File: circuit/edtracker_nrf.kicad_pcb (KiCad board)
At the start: 2 copper layers, 50 x 44 mm, 20 parts, among them M1 NRF24LE1_SMALL, Q1 TPS1101D, SW1 SW_PUSH, SW2 SWITCH_INV, U1 NRF24LE1_PROG, U2 MPU-6050, U3 UART

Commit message: 
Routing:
- net (no net): track 0.00 -> 170.0 mm
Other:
- board text added: "B"
- board text added: "F"

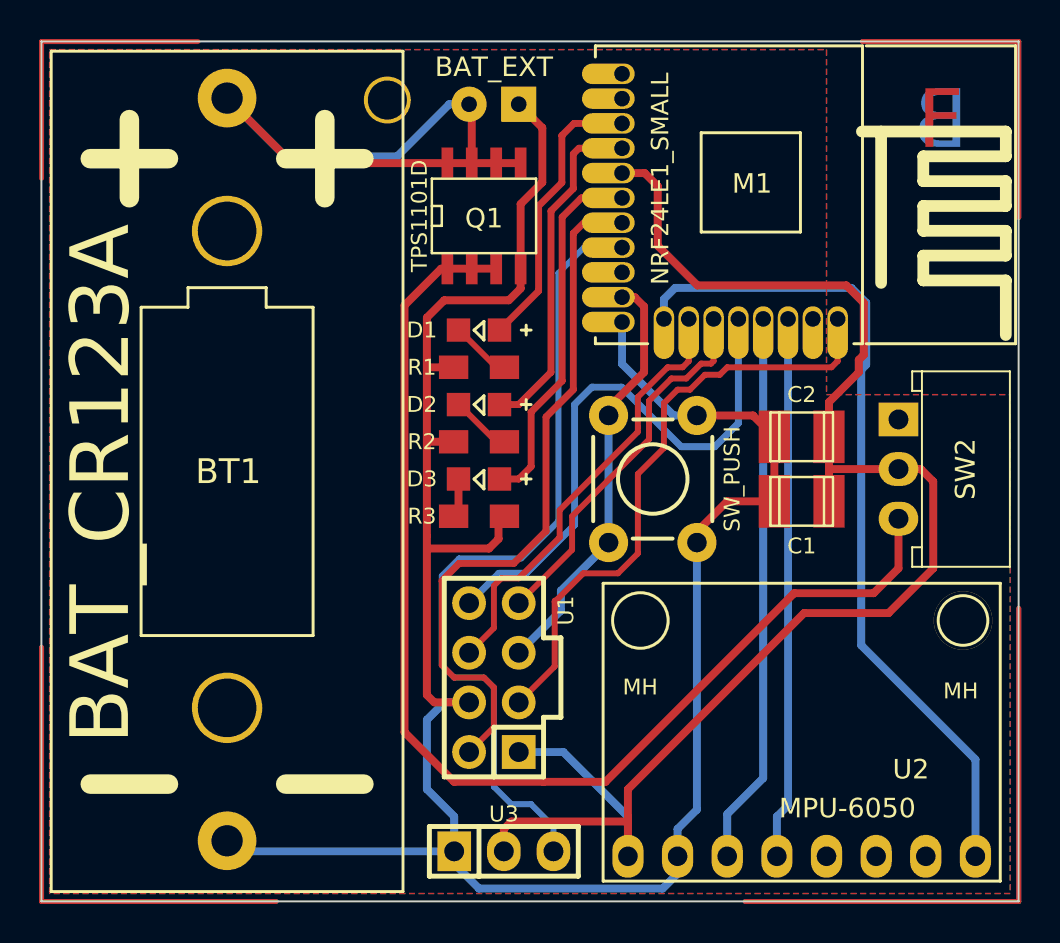
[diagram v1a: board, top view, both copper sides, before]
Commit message: 
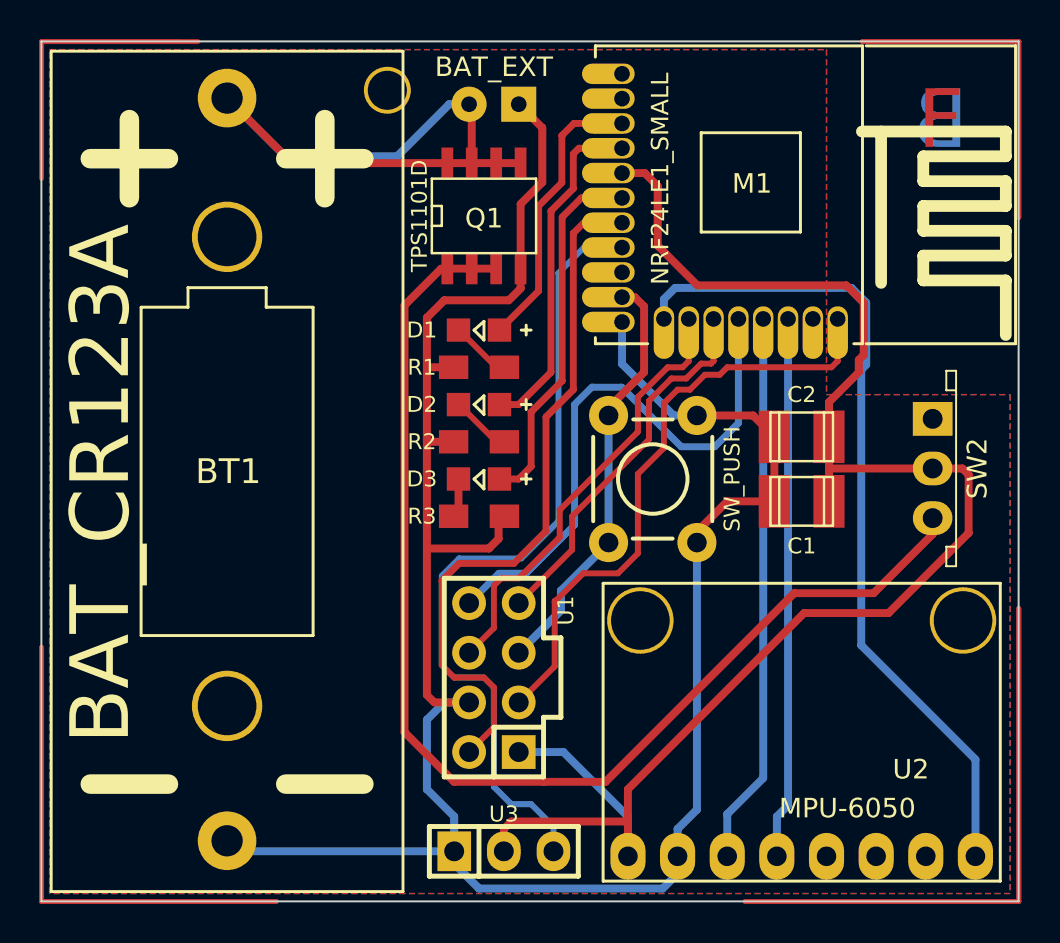
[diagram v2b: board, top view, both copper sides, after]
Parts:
- removed MH (x2): MH30, edtracker_nrf:MountingHole_3mm
- moved SW2 1.75 mm to (95.6, 71.9)
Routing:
- net VCC: track 78.2 -> 81.0 mm
- net Net-(Q1-Pad1): track 60.7 -> 61.5 mm
